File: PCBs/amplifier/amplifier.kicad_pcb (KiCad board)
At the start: 2 copper layers, 200 x 100 mm, 11 parts, among them K1 DIPxx-1Axx-11x, Q4 BS170, Q5 BC547, Q6 BC547, Q9 2SC1815, U1 LM337_TO220

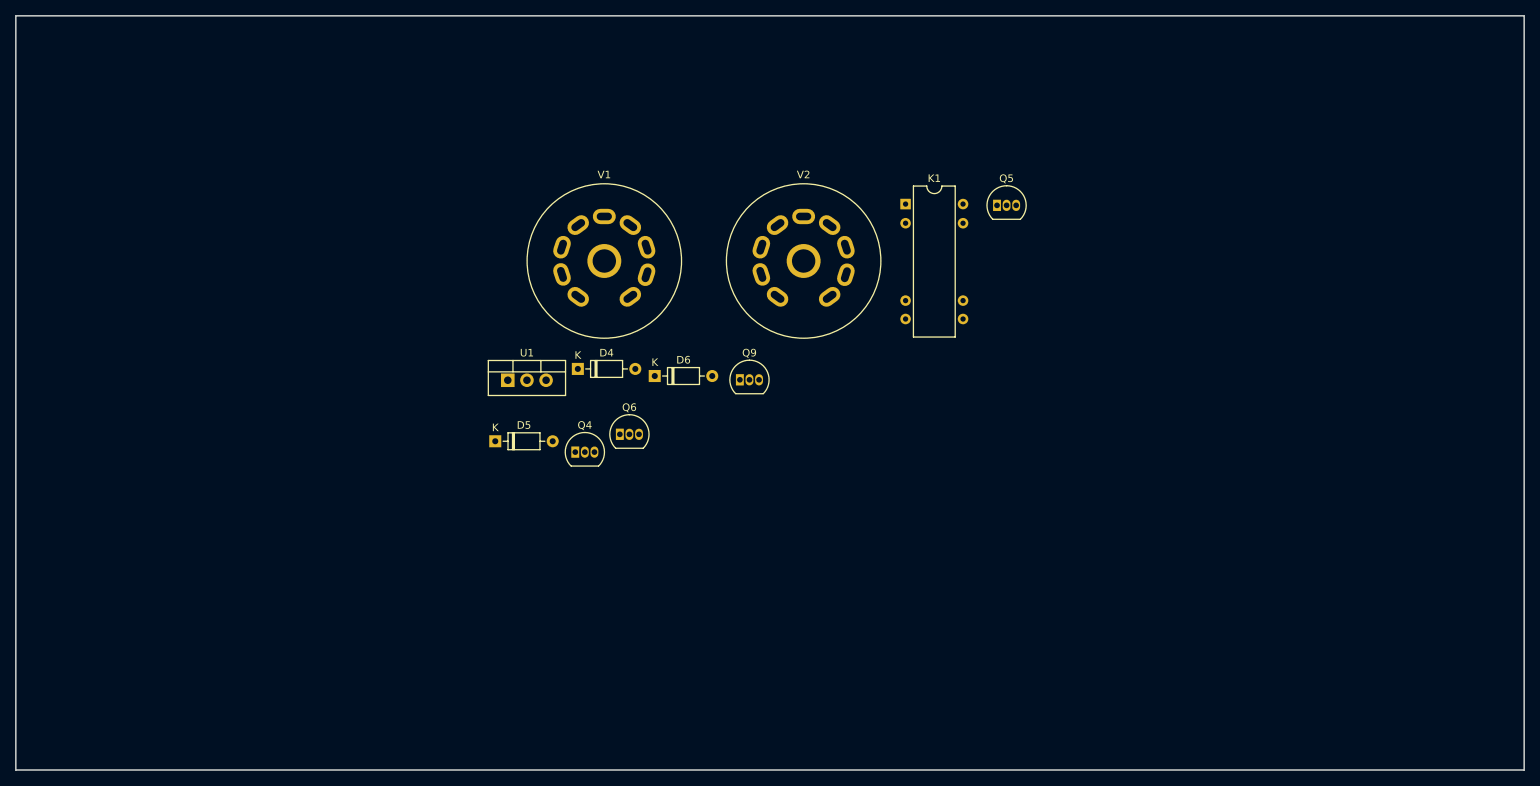
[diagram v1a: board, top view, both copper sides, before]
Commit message: Added correct annotation and started assigning footprints.
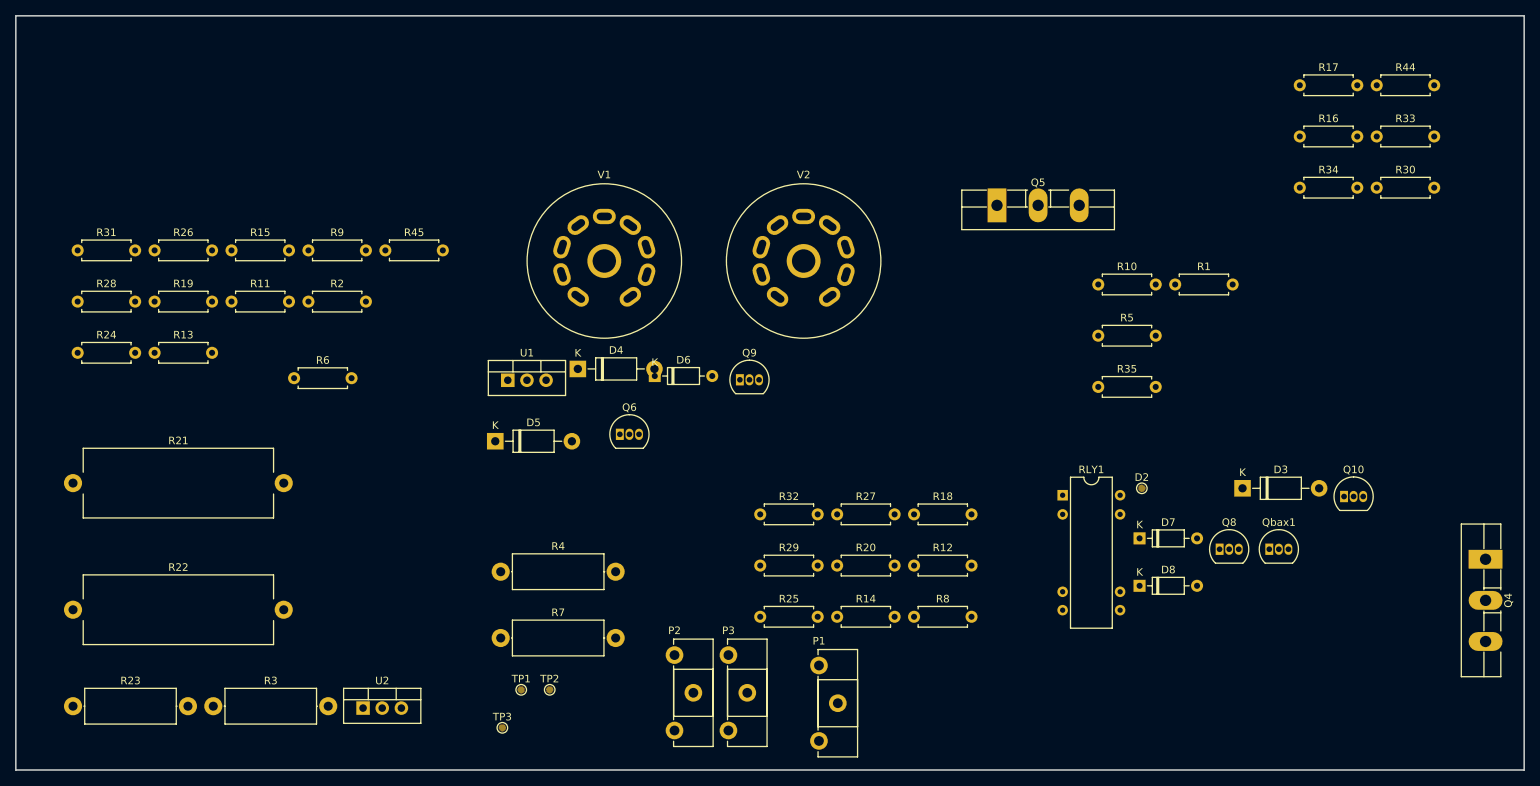
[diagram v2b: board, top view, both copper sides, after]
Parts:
- removed K1: DIPxx-1Axx-11x, Relay_THT:Relay_StandexMeder_DIP_LowProfile
- added D2: UF4007, TestPoint:TestPoint_Pad_D1.0mm, F.Cu at (191.1, 104.0)
- added D3: UF4007, Diode_THT:D_DO-41_SOD81_P10.16mm_Horizontal, F.Cu at (204.5, 104.0)
- added D7: 1N4148, Diode_THT:D_DO-35_SOD27_P7.62mm_Horizontal, F.Cu at (190.8, 110.7)
- added D8: 1N4148, Diode_THT:D_DO-35_SOD27_P7.62mm_Horizontal, F.Cu at (190.8, 116.9)
- added P1: 2k, Potentiometer_THT:Potentiometer_ACP_CA14-H2,5_Horizontal, F.Cu at (148.3, 127.5)
- added P2: 5k, Potentiometer_THT:Potentiometer_ACP_CA14-H2,5_Horizontal, F.Cu at (129.2, 126.1)
- added P3: 5k, Potentiometer_THT:Potentiometer_ACP_CA14-H2,5_Horizontal, F.Cu at (136.3, 126.1)
- added Q10: BC547, Package_TO_SOT_THT:TO-92_Inline, F.Cu at (218.0, 105.1)
- added Q8: BS170, Package_TO_SOT_THT:TO-92_Inline, F.Cu at (201.5, 112.1)
- added Qbax1: 2SC1815, Package_TO_SOT_THT:TO-92_Inline, F.Cu at (208.0, 112.1)
- added R1: 392e, Resistor_THT:R_Axial_DIN0207_L6.3mm_D2.5mm_P7.62mm_Horizontal, F.Cu at (195.6, 77.0)
- added R10: 560e, Resistor_THT:R_Axial_DIN0207_L6.3mm_D2.5mm_P7.62mm_Horizontal, F.Cu at (185.4, 77.0)
- added R11: 18k, Resistor_THT:R_Axial_DIN0207_L6.3mm_D2.5mm_P7.62mm_Horizontal, F.Cu at (70.4, 79.3)
- added R12: 1k, Resistor_THT:R_Axial_DIN0207_L6.3mm_D2.5mm_P7.62mm_Horizontal, F.Cu at (160.9, 114.3)
- added R13: 392e, Resistor_THT:R_Axial_DIN0207_L6.3mm_D2.5mm_P7.62mm_Horizontal, F.Cu at (60.2, 86.0)
- added R14: 2e2, Resistor_THT:R_Axial_DIN0207_L6.3mm_D2.5mm_P7.62mm_Horizontal, F.Cu at (150.7, 121.0)
- added R15: 100e, Resistor_THT:R_Axial_DIN0207_L6.3mm_D2.5mm_P7.62mm_Horizontal, F.Cu at (70.4, 72.5)
- added R16: 20k, Resistor_THT:R_Axial_DIN0207_L6.3mm_D2.5mm_P7.62mm_Horizontal, F.Cu at (212.1, 57.4)
- added R17: 392e, Resistor_THT:R_Axial_DIN0207_L6.3mm_D2.5mm_P7.62mm_Horizontal, F.Cu at (212.1, 50.6)
- added R18: 2e2, Resistor_THT:R_Axial_DIN0207_L6.3mm_D2.5mm_P7.62mm_Horizontal, F.Cu at (160.9, 107.5)
- added R19: 100e, Resistor_THT:R_Axial_DIN0207_L6.3mm_D2.5mm_P7.62mm_Horizontal, F.Cu at (60.2, 79.3)
- added R2: 1k, Resistor_THT:R_Axial_DIN0207_L6.3mm_D2.5mm_P7.62mm_Horizontal, F.Cu at (80.6, 79.3)
- added R20: 1k, Resistor_THT:R_Axial_DIN0207_L6.3mm_D2.5mm_P7.62mm_Horizontal, F.Cu at (150.7, 114.3)
- added R21: 0e22, Resistor_THT:R_Axial_Power_L25.0mm_W9.0mm_P27.94mm, F.Cu at (49.4, 103.3)
- added R22: 0e22, Resistor_THT:R_Axial_Power_L25.0mm_W9.0mm_P27.94mm, F.Cu at (49.4, 120.1)
- added R23: 10e, Resistor_THT:R_Axial_DIN0414_L11.9mm_D4.5mm_P15.24mm_Horizontal, F.Cu at (49.4, 132.9)
- added R24: 182e, Resistor_THT:R_Axial_DIN0207_L6.3mm_D2.5mm_P7.62mm_Horizontal, F.Cu at (50.0, 86.0)
- added R25: 1k5, Resistor_THT:R_Axial_DIN0207_L6.3mm_D2.5mm_P7.62mm_Horizontal, F.Cu at (140.5, 121.0)
- added R26: 182e, Resistor_THT:R_Axial_DIN0207_L6.3mm_D2.5mm_P7.62mm_Horizontal, F.Cu at (60.2, 72.5)
- added R27: 3k3, Resistor_THT:R_Axial_DIN0207_L6.3mm_D2.5mm_P7.62mm_Horizontal, F.Cu at (150.7, 107.5)
- added R28: 1M, Resistor_THT:R_Axial_DIN0207_L6.3mm_D2.5mm_P7.62mm_Horizontal, F.Cu at (50.0, 79.3)
- added R29: 1M, Resistor_THT:R_Axial_DIN0207_L6.3mm_D2.5mm_P7.62mm_Horizontal, F.Cu at (140.5, 114.3)
- added R3: 150k, Resistor_THT:R_Axial_DIN0414_L11.9mm_D4.5mm_P15.24mm_Horizontal, F.Cu at (68.0, 132.9)
- added R30: 330k, Resistor_THT:R_Axial_DIN0207_L6.3mm_D2.5mm_P7.62mm_Horizontal, F.Cu at (222.3, 64.2)
- added R31: 10M, Resistor_THT:R_Axial_DIN0207_L6.3mm_D2.5mm_P7.62mm_Horizontal, F.Cu at (50.0, 72.5)
- added R32: 1k, Resistor_THT:R_Axial_DIN0207_L6.3mm_D2.5mm_P7.62mm_Horizontal, F.Cu at (140.5, 107.5)
- added R33: 100k, Resistor_THT:R_Axial_DIN0207_L6.3mm_D2.5mm_P7.62mm_Horizontal, F.Cu at (222.3, 57.4)
- added R34: 100k, Resistor_THT:R_Axial_DIN0207_L6.3mm_D2.5mm_P7.62mm_Horizontal, F.Cu at (212.1, 64.2)
- added R35: 100k, Resistor_THT:R_Axial_DIN0207_L6.3mm_D2.5mm_P7.62mm_Horizontal, F.Cu at (185.4, 90.6)
- added R4: 150k, Resistor_THT:R_Axial_DIN0414_L11.9mm_D4.5mm_P15.24mm_Horizontal, F.Cu at (106.1, 115.1)
- added R44: 4e7, Resistor_THT:R_Axial_DIN0207_L6.3mm_D2.5mm_P7.62mm_Horizontal, F.Cu at (222.3, 50.6)
- added R45: 100e, Resistor_THT:R_Axial_DIN0207_L6.3mm_D2.5mm_P7.62mm_Horizontal, F.Cu at (90.8, 72.5)
- added R5: 1k, Resistor_THT:R_Axial_DIN0207_L6.3mm_D2.5mm_P7.62mm_Horizontal, F.Cu at (185.4, 83.8)
- added R6: 100e, Resistor_THT:R_Axial_DIN0207_L6.3mm_D2.5mm_P7.62mm_Horizontal, F.Cu at (78.7, 89.4)
- added R7: 22k, Resistor_THT:R_Axial_DIN0414_L11.9mm_D4.5mm_P15.24mm_Horizontal, F.Cu at (106.1, 123.9)
- added R8: 2k43, Resistor_THT:R_Axial_DIN0207_L6.3mm_D2.5mm_P7.62mm_Horizontal, F.Cu at (160.9, 121.0)
- added R9: 274e, Resistor_THT:R_Axial_DIN0207_L6.3mm_D2.5mm_P7.62mm_Horizontal, F.Cu at (80.6, 72.5)
- added RLY1: LR-24, Relay_THT:Relay_StandexMeder_DIP_LowProfile, F.Cu at (180.6, 104.9)
- added TP1: 1.6V, TestPoint:TestPoint_Pad_D1.0mm, F.Cu at (108.9, 130.7)
- added TP2: 1.6V, TestPoint:TestPoint_Pad_D1.0mm, F.Cu at (112.6, 130.7)
- added TP3: 1.6V, TestPoint:TestPoint_Pad_D1.0mm, F.Cu at (106.4, 135.8)
- added U2: LM317, Package_TO_SOT_THT:TO-220-3_Vertical, F.Cu at (87.9, 133.2)
- D4, D5: value 1N4148 -> 1N4001; footprint Diode_THT:D_DO-35_SOD27_P7.62mm_Horizontal -> Diode_THT:D_DO-41_SOD81_P10.16mm_Horizontal
- Q4: value BS170 -> 2SC5200; footprint Package_TO_SOT_THT:TO-92_Inline -> Package_TO_SOT_THT:TO-264_Vertical
- Q5: value BC547 -> 2SC5200; footprint Package_TO_SOT_THT:TO-92_Inline -> Package_TO_SOT_THT:TO-264_Vertical
- Q6: value BC547 -> BC550
- Q9: value 2SC1815 -> BC547
- U1: value LM337_TO220 -> LM337
- moved Q4 121.5 mm to (236.7, 113.4), turned to 270 degrees
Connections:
- D4 pad 1: Net-(C12-Pad1) -> Net-(C12-Pad2)
- D4 pad 2: Net-(D4-Pad2) -> -38V
- D5 pad 1: Net-(C13-Pad1) -> +42V
- D5 pad 2: Net-(D5-Pad2) -> Net-(C17-Pad1)
- D6 pad 1: Net-(C12-Pad1) -> Net-(C17-Pad1)
- D6 pad 2: Net-(C13-Pad1) -> Net-(D6-Pad2)
- Q4 pad 1: Net-(D4-Pad2) -> Net-(Q4-Pad1)
- Q4 pad 3: GND -> Net-(Q4-Pad3)
- Q5 pad 3: Net-(C15-Pad2) -> -38V
- Q6 pad 1: Net-(Q5-Pad1) -> Net-(Q6-Pad1)
- Q6 pad 2: Net-(Q5-Pad2) -> Net-(Q6-Pad2)
- Q6 pad 3: Net-(Q5-Pad2) -> Net-(Q6-Pad3)
- Q9 pad 2: Net-(Q11-Pad2) -> Net-(C20-Pad2)
- Q9 pad 3: Net-(Q11-Pad2) -> Net-(Q10-Pad2)
- U1 pad 3: Net-(C2-Pad2) (its old number) -> Net-(C12-Pad2)
- V1 pad 3: Net-(Q1-Pad1) -> Net-(J4-Pad1)
- V1 pad 8: Net-(Q1-Pad1) -> Net-(Q6-Pad1)

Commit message: amp. sch. done, all footprints added.
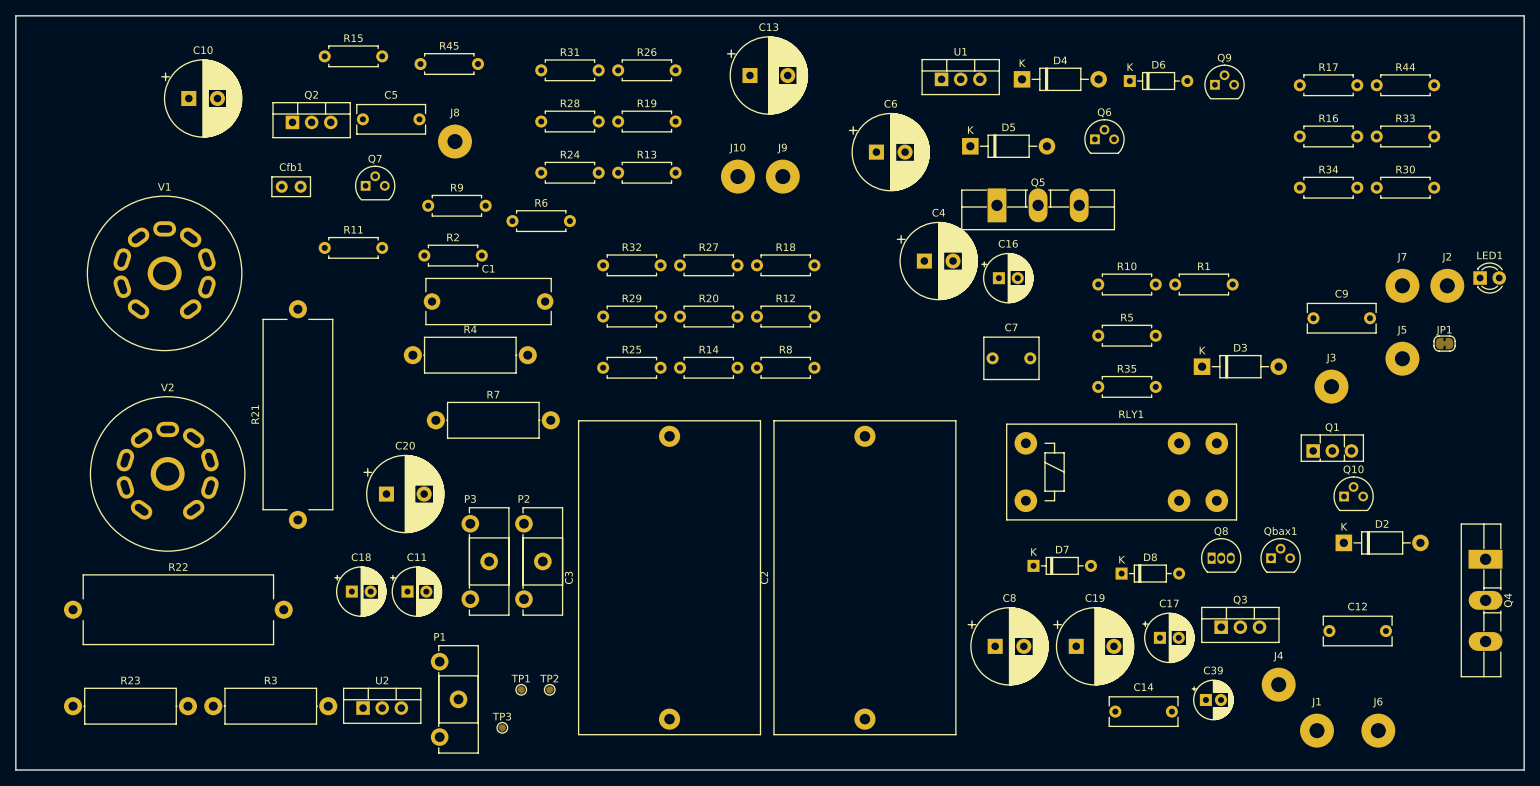
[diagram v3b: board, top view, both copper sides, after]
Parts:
- added C1: 100n, Capacitor_THT:C_Rect_L16.5mm_W6.0mm_P15.00mm_MKT, F.Cu at (97.0, 79.2)
- added C10: 270u, Capacitor_THT:CP_Radial_D10.0mm_P3.80mm, F.Cu at (64.8, 52.3)
- added C11: 10u, Capacitor_THT:CP_Radial_D6.3mm_P2.50mm, F.Cu at (93.8, 117.7)
- added C12: 100n, Capacitor_THT:C_Rect_L9.0mm_W3.8mm_P7.50mm_MKT, F.Cu at (216.0, 122.9)
- added C13: 47u, Capacitor_THT:CP_Radial_D10.0mm_P5.00mm, F.Cu at (139.2, 49.3)
- added C14: 100n, Capacitor_THT:C_Rect_L9.0mm_W3.8mm_P7.50mm_MKT, F.Cu at (187.6, 133.6)
- added C16: 10u, Capacitor_THT:CP_Radial_D6.3mm_P2.50mm, F.Cu at (172.2, 76.1)
- added C17: 10u, Capacitor_THT:CP_Radial_D6.3mm_P2.50mm, F.Cu at (193.5, 123.8)
- added C18: 22u, Capacitor_THT:CP_Radial_D6.3mm_P2.50mm, F.Cu at (86.4, 117.7)
- added C19: 47u, Capacitor_THT:CP_Radial_D10.0mm_P5.00mm, F.Cu at (182.5, 125.0)
- added C2: 3u3, Capacitor_THT:C_Rect_L41.5mm_W24.0mm_P37.50mm_MKS4, F.Cu at (154.4, 134.6)
- added C20: 47u, Capacitor_THT:CP_Radial_D10.0mm_P5.00mm, F.Cu at (91.0, 104.8)
- added C3: 3u3, Capacitor_THT:C_Rect_L41.5mm_W24.0mm_P37.50mm_MKS4, F.Cu at (128.5, 134.6)
- added C39: 10u, Capacitor_THT:CP_Radial_D5.0mm_P2.00mm, F.Cu at (199.6, 132.1)
- added C4: 270u, Capacitor_THT:CP_Radial_D10.0mm_P3.80mm, F.Cu at (162.3, 73.9)
- added C5: 100n, Capacitor_THT:C_Rect_L9.0mm_W3.8mm_P7.50mm_MKT, F.Cu at (87.9, 55.1)
- added C6: 270u, Capacitor_THT:CP_Radial_D10.0mm_P3.80mm, F.Cu at (156.0, 59.4)
- added C7: 100n, Capacitor_THT:C_Rect_L7.2mm_W5.5mm_P5.00mm_FKS2_FKP2_MKS2_MKP2, F.Cu at (171.4, 86.8)
- added C8: 270u, Capacitor_THT:CP_Radial_D10.0mm_P3.80mm, F.Cu at (171.7, 125.0)
- added C9: 100n, Capacitor_THT:C_Rect_L9.0mm_W3.8mm_P7.50mm_MKT, F.Cu at (213.9, 81.5)
- added Cfb1: 56p, Capacitor_THT:C_Disc_D5.0mm_W2.5mm_P2.50mm, F.Cu at (77.1, 64.0)
- added J1: 6V3A, Connector_Wire:SolderWirePad_single_2mmDrill, F.Cu at (214.4, 136.1)
- added J10: LS1A, Connector_Wire:SolderWirePad_single_2mmDrill, F.Cu at (137.6, 62.7)
- added J2: 6V3B, Connector_Wire:SolderWirePad_single_2mmDrill, F.Cu at (231.7, 77.2)
- added J3: AUX-IN, Connector_Wire:SolderWirePad_single_2mmDrill, F.Cu at (216.3, 90.5)
- added J4: AUX-IN-GND, Connector_Wire:SolderWirePad_single_2mmDrill, F.Cu at (209.3, 130.0)
- added J5: +38V, Connector_Wire:SolderWirePad_single_2mmDrill, F.Cu at (225.7, 86.8)
- added J6: -38V, Connector_Wire:SolderWirePad_single_2mmDrill, F.Cu at (222.5, 136.1)
- added J7: GND, Connector_Wire:SolderWirePad_single_2mmDrill, F.Cu at (225.7, 77.2)
- added J8: +310V, Connector_Wire:SolderWirePad_single_2mmDrill, F.Cu at (100.1, 58.0)
- added J9: LS1B, Connector_Wire:SolderWirePad_single_2mmDrill, F.Cu at (143.5, 62.7)
- added JP1: bridge, Jumper:SolderJumper-2_P1.3mm_Bridged_RoundedPad1.0x1.5mm, F.Cu at (231.3, 84.8)
- added LED1: RED, LED_THT:LED_D3.0mm, F.Cu at (236.0, 76.1)
- added Q1: BD139, Package_TO_SOT_THT:TO-126_Vertical, F.Cu at (213.9, 99.1)
- added Q2: 2SC2073, Package_TO_SOT_THT:TO-220-3_Vertical, F.Cu at (78.5, 55.5)
- added Q3: 2SA940, Package_TO_SOT_THT:TO-220-3_Vertical, F.Cu at (201.7, 122.4)
- added Q7: BC550, Package_TO_SOT_THT:TO-92, F.Cu at (88.2, 63.9)
- D2: footprint TestPoint:TestPoint_Pad_D1.0mm -> Diode_THT:D_DO-41_SOD81_P10.16mm_Horizontal
- Q10, Q6, Q9, Qbax1: footprint Package_TO_SOT_THT:TO-92_Inline -> Package_TO_SOT_THT:TO-92
- RLY1: footprint Relay_THT:Relay_StandexMeder_DIP_LowProfile -> Relay_THT:Relay_SPST_Schrack-RP-II-1-16A-FormA_RM5mm
- moved V2 88.9 mm to (65.4, 106.9)
- moved D5 74.1 mm to (168.4, 58.7)
- moved D6 74.1 mm to (189.6, 50.0)
- moved Q6 74.1 mm to (184.9, 57.7)
- moved Q9 74.1 mm to (200.8, 50.5)
- moved D4 70.3 mm to (175.3, 49.8)
- moved U1 70.0 mm to (164.6, 49.8)
- moved R13 65.9 mm to (121.7, 62.2)
- moved R19 65.9 mm to (121.7, 55.4)
- moved R24 65.9 mm to (111.5, 62.2)
- moved R26 65.9 mm to (121.7, 48.6)
- moved R28 65.9 mm to (111.5, 55.4)
- moved R31 65.9 mm to (111.5, 48.6)
- moved V1 58.3 mm to (65.0, 80.3)
- moved P1 50.3 mm to (98.0, 127.0)
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
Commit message: Rough component placement amp. pcb.
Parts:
- P1, P2, P3: footprint Potentiometer_THT:Potentiometer_ACP_CA14-H2,5_Horizontal -> Potentiometer_THT:Potentiometer_Bourns_3266Y_Vertical
- moved J2 163.9 mm to (74.8, 124.6)
- moved J5 149.7 mm to (80.9, 124.6)
- moved LED1 147.4 mm to (96.1, 122.7)
- moved Q2 145.0 mm to (221.8, 77.6), turned to 270 degrees
- moved J7 144.8 mm to (91.5, 131.7)
- moved C14 141.4 mm to (72.0, 52.2)
- moved J1 141.2 mm to (73.3, 131.7)
- moved R21 138.5 mm to (213.6, 74.5), turned to 180 degrees
- moved R44 138.4 mm to (111.4, 133.3)
- moved R22 137.5 mm to (186.9, 118.9)
- moved J3 137.2 mm to (85.5, 131.7)
- moved J6 136.0 mm to (87.0, 124.6)
- moved R23 133.9 mm to (181.2, 109.4), turned to 90 degrees
- moved C10 133.7 mm to (178.0, 123.3), turned to 270 degrees
- moved J4 130.0 mm to (79.4, 131.7)
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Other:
- board size 200 x 100 mm -> 160 x 90 mm
